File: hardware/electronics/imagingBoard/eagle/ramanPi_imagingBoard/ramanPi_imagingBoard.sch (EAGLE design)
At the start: 13 parts

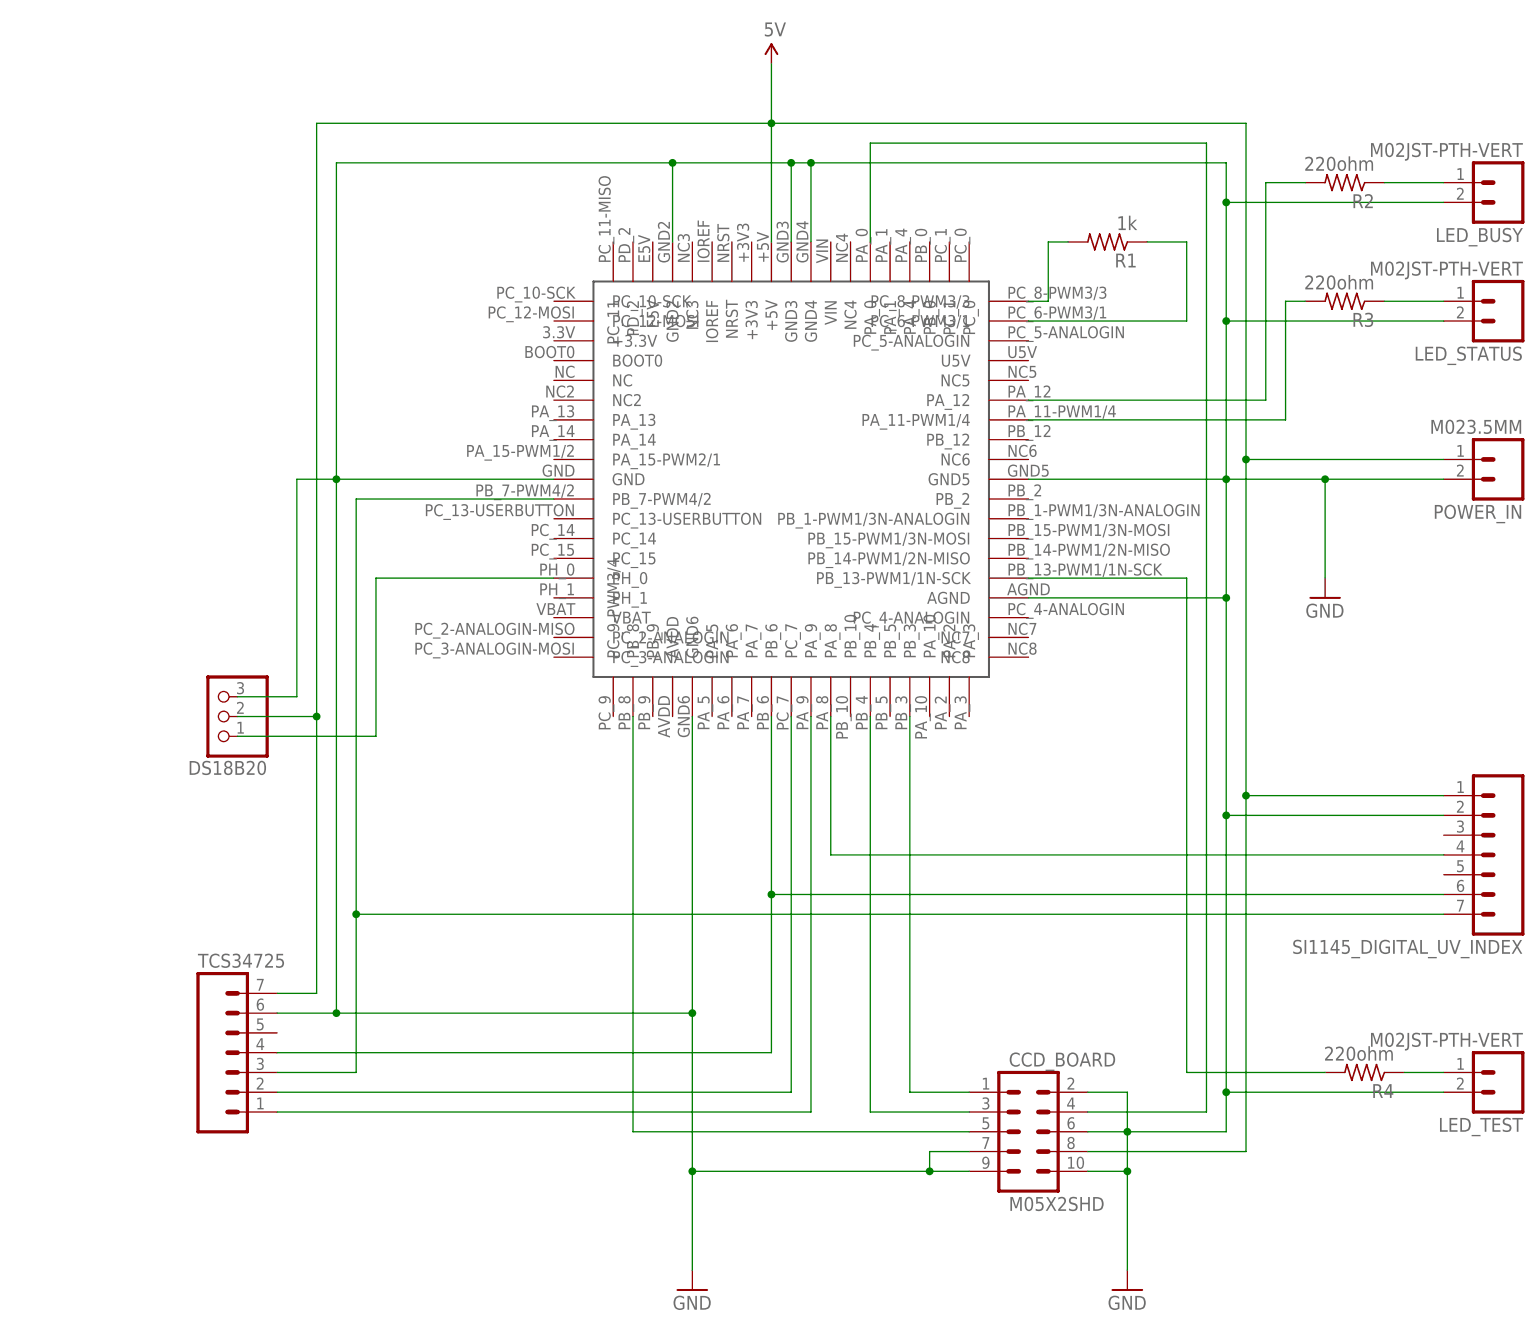
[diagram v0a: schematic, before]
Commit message: imagingBoard updated
updated pin configuration for remote ccd board to match with new pinout
added ground plane and decoupling caps
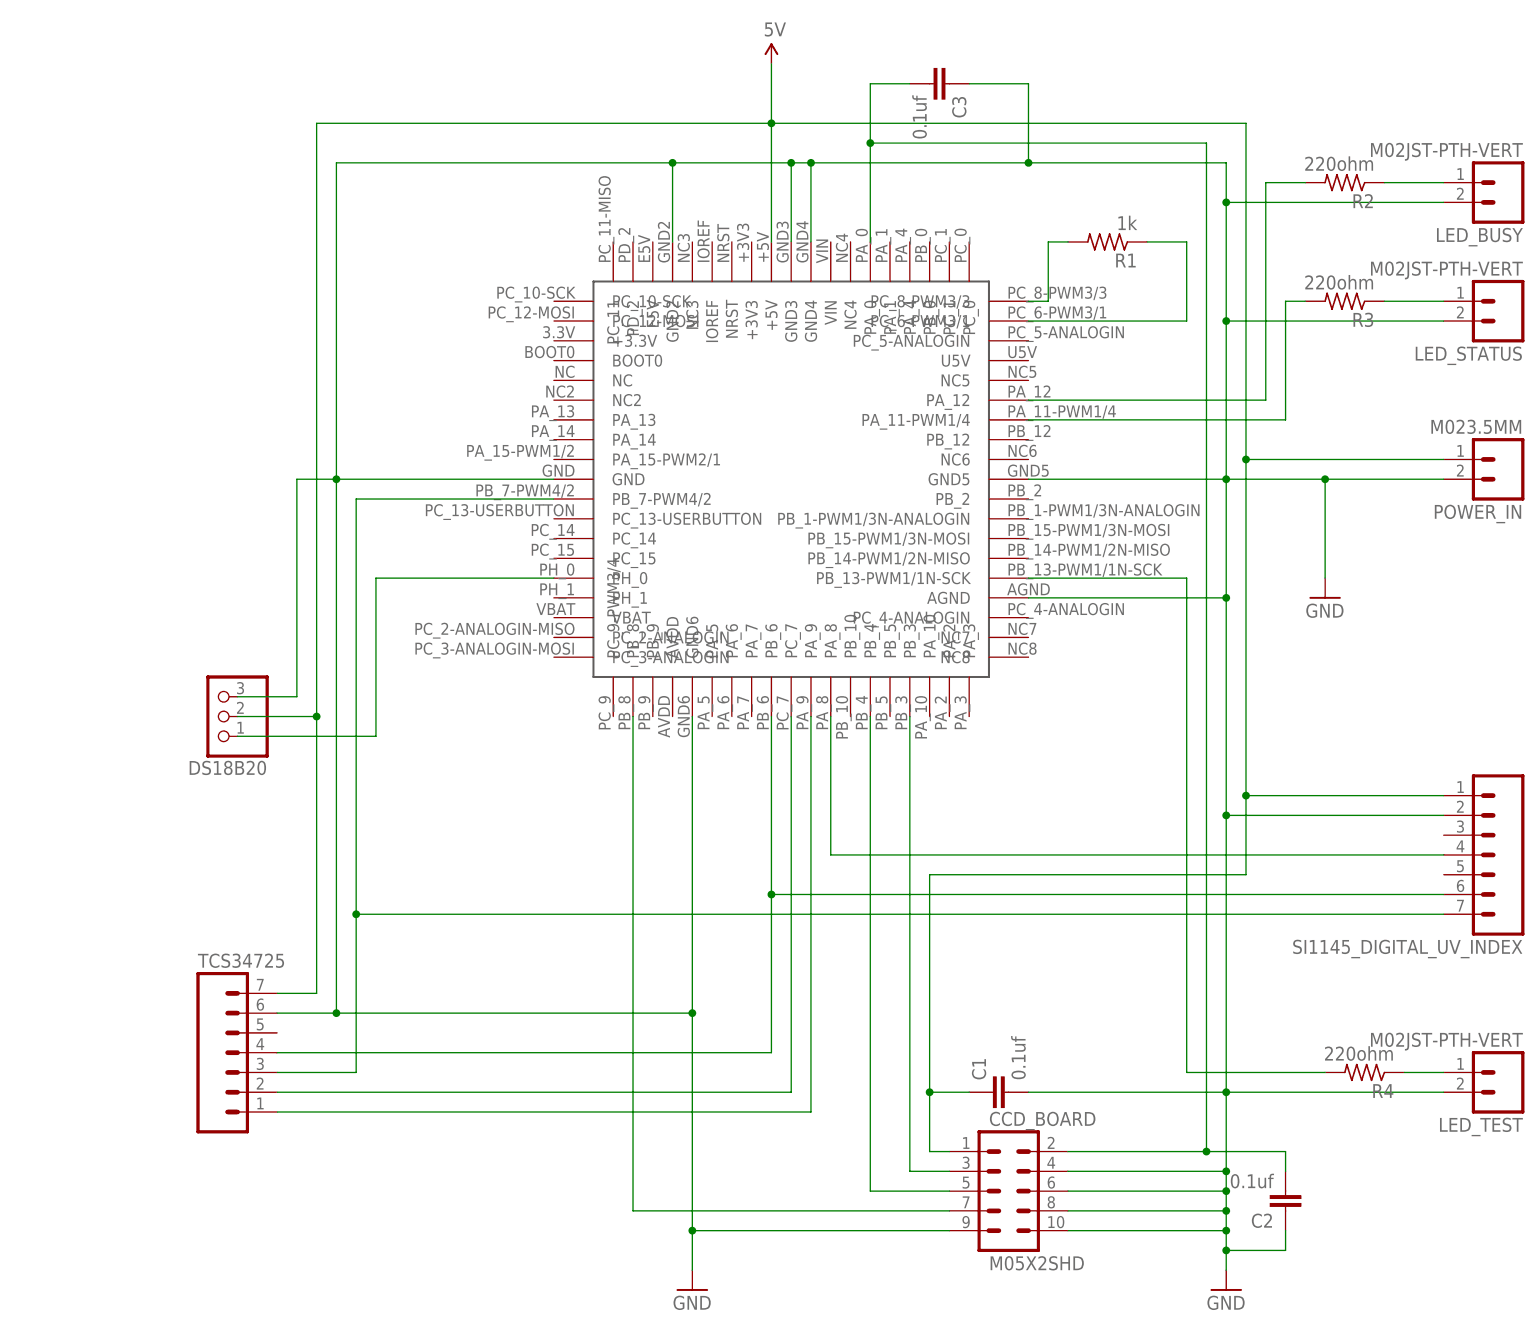
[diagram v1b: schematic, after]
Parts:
- added C1, C2, C3: 0.1uf, SparkFun-Capacitors:CAP1210
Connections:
- removed net N$3: CCD_BOARD.1, U$1.PB_3
- new net N$20: CCD_BOARD.3, U$1.PB_3
- net 5V: now also C1.1, CCD_BOARD.1; no longer CCD_BOARD.8
- net GND: now also C1.2, C2.1, C3.1, CCD_BOARD.4, CCD_BOARD.8; no longer CCD_BOARD.2, CCD_BOARD.7
- net N$1: now also CCD_BOARD.7; no longer CCD_BOARD.5
- net N$2: now also CCD_BOARD.5; no longer CCD_BOARD.3
- net N$9: now also C2.2, C3.2, CCD_BOARD.2; no longer CCD_BOARD.4
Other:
- moved on the sheet: CCD_BOARD
